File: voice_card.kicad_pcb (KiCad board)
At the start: 2 copper layers, 119.3 x 38 mm, 209 parts, among them J1 PCI_11_49, Q1 MMBF4391LT1G, Q10 DMMT3906, Q11 BC857BS, Q2 2N3904, Q3 BCM847, Q4 DMMT3904, Q5 DMMT3906, Q6 MMBF4391LT1G, Q7 BCM847, Q8 2N3904, Q9 DMMT3904, U1 TL074-, U10 TL072-, U11 TL074-, U12 NE555, U13 LM311M, U14 CD4052, U15 TL072-, U16 TL072-, U17 LM13700, U18 LM13700, U19 LM13700, U2 TL074-, U20 TL072-, U3 NE555, U4 LF351, U5 TL072-, U6 LM311M, U7 CD4052, U8 TL074-, U9 LF351

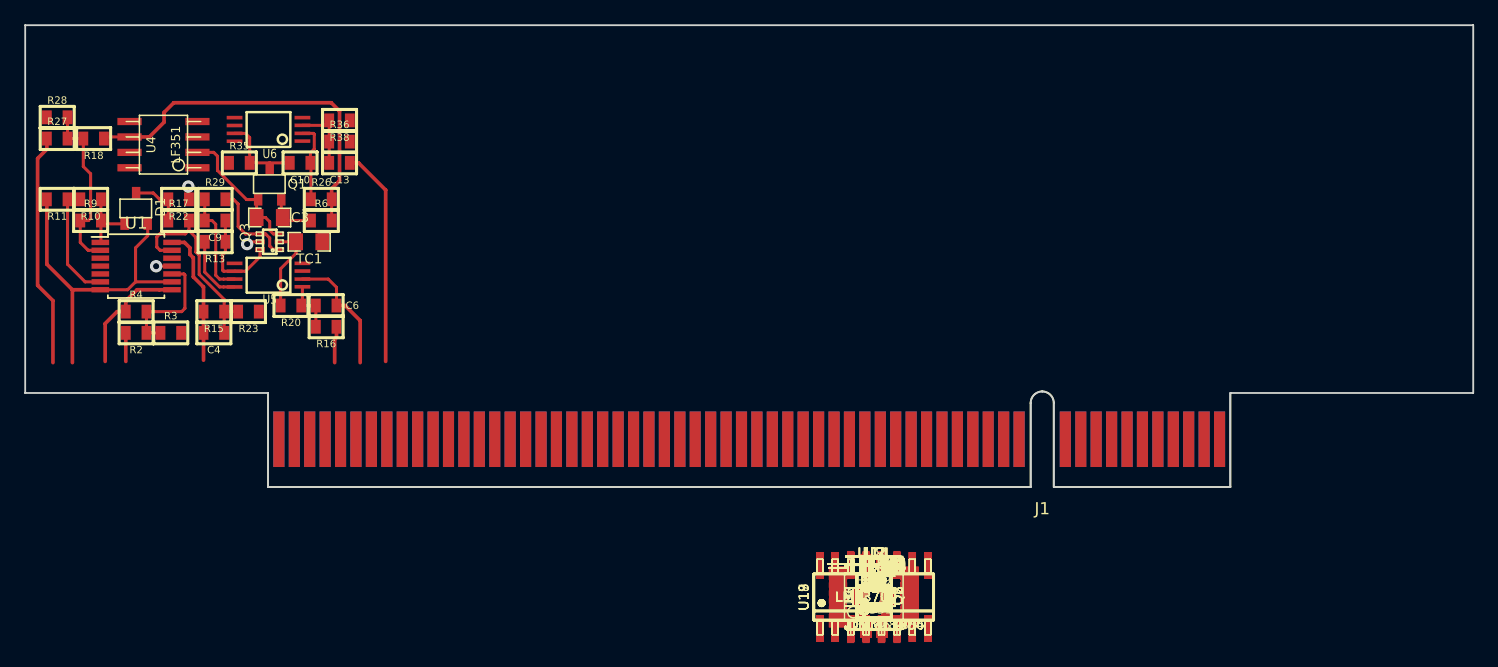
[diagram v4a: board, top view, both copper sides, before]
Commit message: starting to place VCO2 components
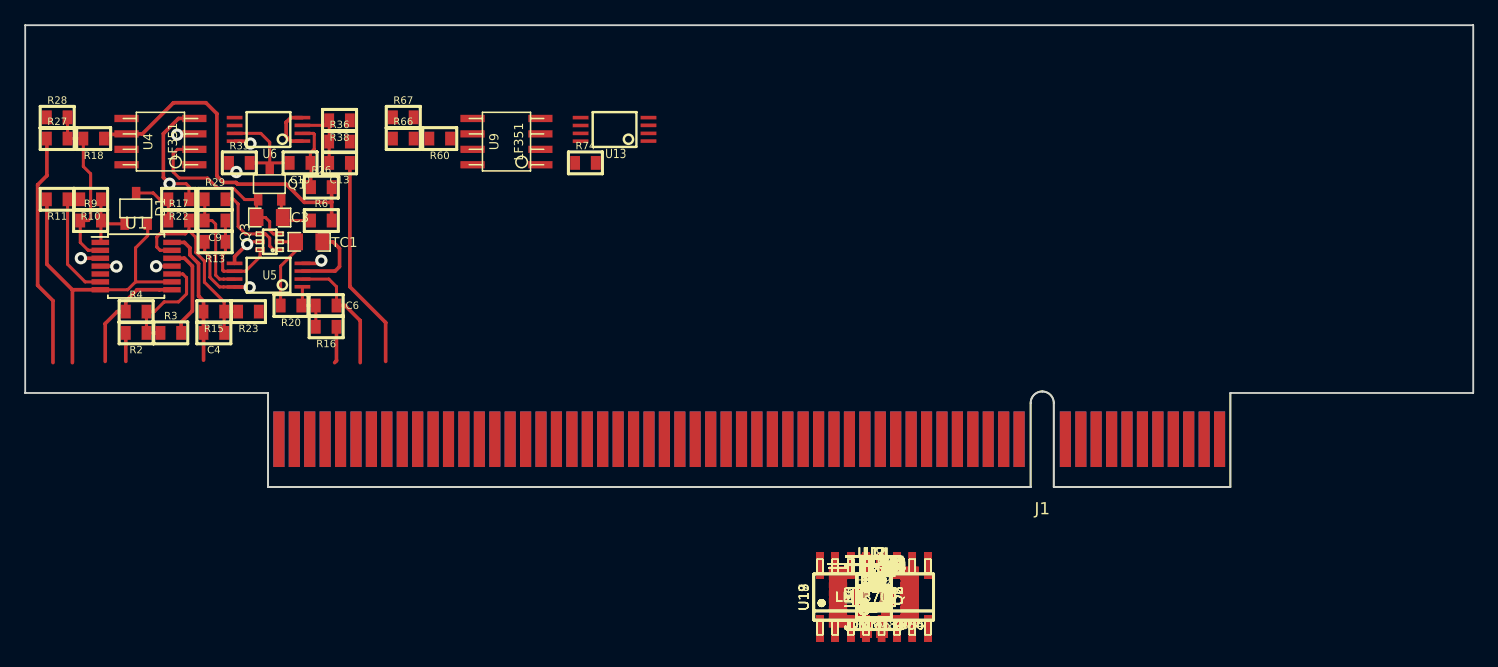
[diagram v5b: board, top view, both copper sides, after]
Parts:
- moved R67 55.3 mm to (109.8, 65.5)
- moved R66 54.1 mm to (109.8, 67.2)
- moved R60 52.0 mm to (112.8, 67.2), turned to 180 degrees
- moved U9 48.2 mm to (118.2, 67.5), turned to 90 degrees
- moved U13 44.0 mm to (127.2, 66.5), turned to 90 degrees
- moved R74 42.9 mm to (124.8, 69.2)
- moved R26 1.00 mm to (103.0, 71.2)
- moved U4 0.35 mm to (89.8, 67.5)
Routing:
- net GND: track 1.14 -> 21.4 mm, vias 1 -> 4
- net -12V: track 2.38 -> 17.3 mm, vias 2 -> 3
- net Net-(C3-Pad1): track 11.7 -> 15.7 mm
- net +12V: track 5.46 -> 9.44 mm, vias 0 -> 3
- net Net-(C10-Pad2): track 7.25 -> 9.32 mm
- net Net-(R18-Pad1): track 30.8 -> 29.3 mm
- net Net-(C10-Pad1): track 6.51 -> 5.51 mm
- net Net-(R2-Pad1): track 10.0 -> 9.47 mm

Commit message: VCO1 and VCO2 rough layout done. Starting to place VCF and VCA components
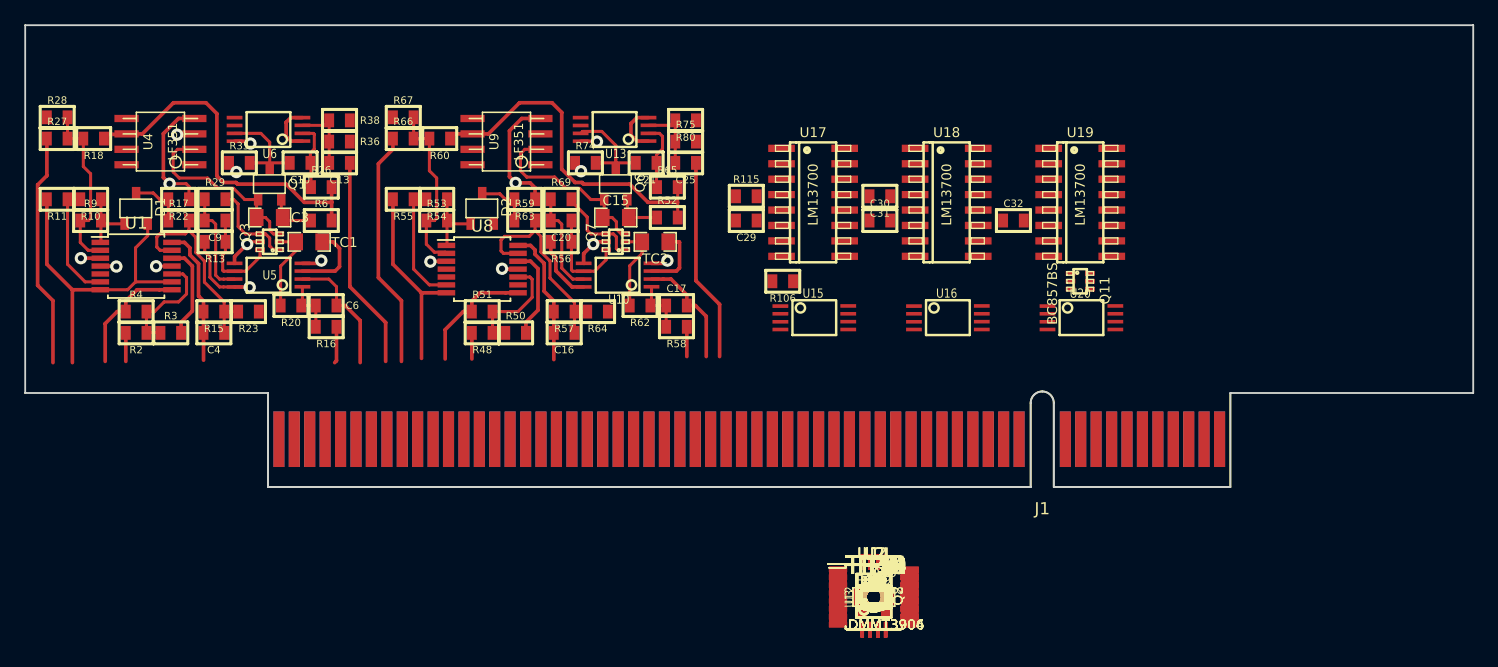
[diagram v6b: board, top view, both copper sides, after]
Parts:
- moved R55 50.7 mm to (109.8, 72.2), turned to 180 degrees
- moved R54 48.7 mm to (112.5, 72.2), turned to 180 degrees
- moved R53 47.5 mm to (112.5, 74.0)
- moved D2 45.4 mm to (116.2, 73.0)
- moved R63 43.6 mm to (119.8, 72.2), turned to 180 degrees
- moved R59 42.3 mm to (119.8, 74.0)
- moved R80 42.2 mm to (133.0, 65.8), turned to 180 degrees
- moved U8 42.1 mm to (116.2, 78.0)
- moved R69 41.7 mm to (122.8, 72.2)
- moved R75 40.6 mm to (133.0, 67.5)
- moved C21 40.4 mm to (129.8, 69.2), turned to 180 degrees
- moved C20 40.3 mm to (122.8, 74.0), turned to 180 degrees
- moved Q6 40.1 mm to (127.2, 71.0)
- moved R51 39.9 mm to (116.2, 81.5)
- moved R56 39.0 mm to (122.8, 75.8), turned to 180 degrees
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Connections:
- U8 pad 10: GND -> Net-(R48-Pad1)
- U8 pad 12: Net-(R48-Pad1) -> GND
- U8 pad 13: VCO2_SAW -> Net-(C16-Pad1)
- U8 pad 14: VCO2_PULSE -> VCO2_TRI
- U8 pad 8: VCO2_TRI -> VCO2_PULSE
- U8 pad 9: Net-(C16-Pad1) -> VCO2_SAW
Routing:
- net Net-(R52-Pad2): track 0.00 -> 29.3 mm
- net VCO2_TRI_SHAPE: track 0.00 -> 19.6 mm
- net GND: track 21.4 -> 39.7 mm, vias 4 -> 7
- net -12V: track 17.3 -> 34.4 mm, vias 3 -> 6
- net Net-(C16-Pad1): track 0.00 -> 17.1 mm
- net VCO2_SYNC_IN: track 0.00 -> 16.8 mm
- net VCO2_SAW: track 0.00 -> 16.1 mm
- net Net-(C15-Pad1): track 0.00 -> 15.4 mm
- net Net-(R53-Pad1): track 0.00 -> 14.7 mm
- net VCO2_TRI: track 0.00 -> 11.2 mm
- net VCO2_PULSE: track 0.00 -> 10.2 mm
- net Net-(R54-Pad2): track 0.00 -> 10.0 mm
- net VCO2_PITCH_CV: track 0.00 -> 9.60 mm
- net Net-(R48-Pad1): track 0.00 -> 9.28 mm
- net Net-(C21-Pad2): track 0.00 -> 9.13 mm
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
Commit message: routing vcf almost done, then need to do VCA and expo converter
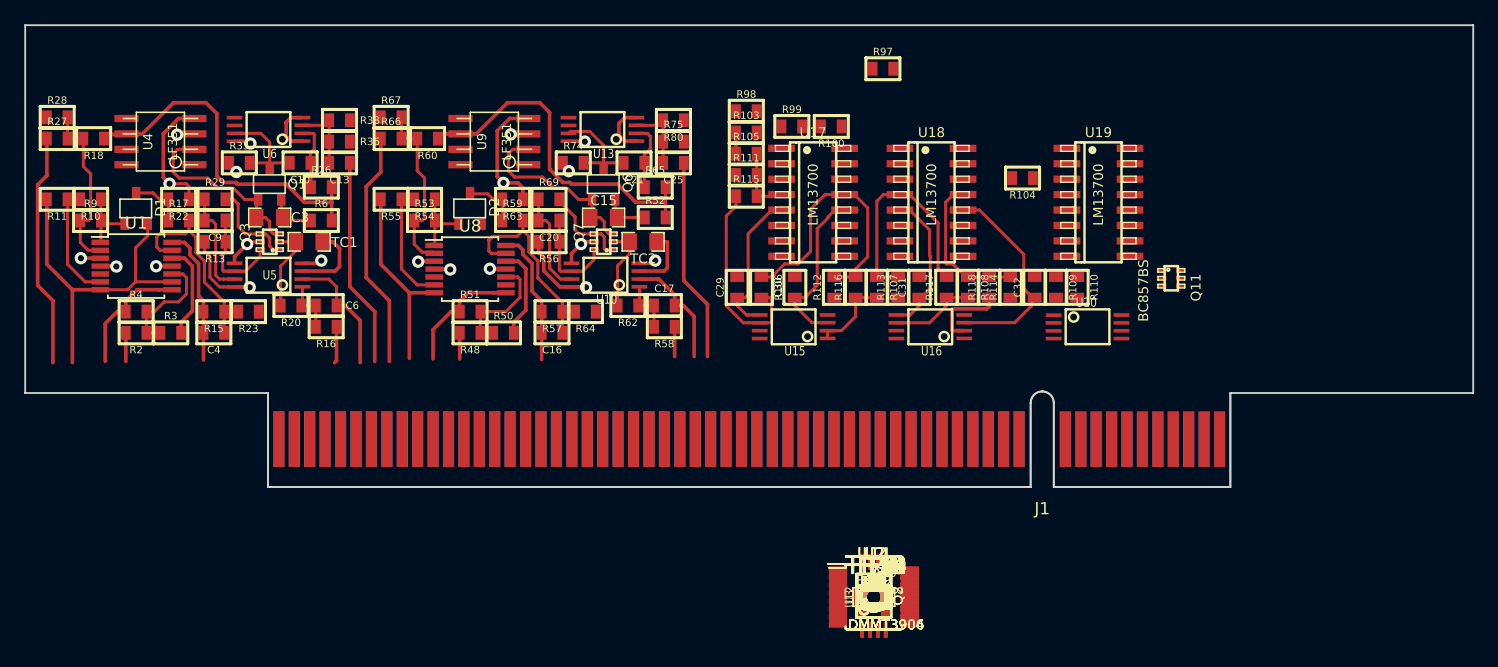
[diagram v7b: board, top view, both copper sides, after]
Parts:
- moved R97 43.5 mm to (149.2, 61.5)
- moved R98 41.4 mm to (138.0, 65.0)
- moved R103 39.7 mm to (138.0, 66.8)
- moved R99 39.3 mm to (141.8, 66.2)
- moved R100 38.9 mm to (145.0, 66.2), turned to 180 degrees
- moved R105 38.0 mm to (138.0, 68.5)
- moved R104 36.6 mm to (160.8, 70.5), turned to 180 degrees
- moved R111 36.3 mm to (138.0, 70.2)
- moved R110 30.5 mm to (165.2, 79.5), turned to 270 degrees
- moved R109 29.6 mm to (163.5, 79.5), turned to 270 degrees
- moved R114 27.9 mm to (159.8, 79.5), turned to 90 degrees
- moved R118 27.2 mm to (158.0, 79.5), turned to 90 degrees
- moved R108 26.7 mm to (156.2, 79.5), turned to 270 degrees
- moved R117 26.2 mm to (154.5, 79.5), turned to 90 degrees
- moved R112 25.7 mm to (145.2, 79.5), turned to 90 degrees
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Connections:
- U15 pad 1: Net-(R106-Pad2) -> Net-(R107-Pad2)
- U15 pad 2: Net-(R106-Pad2) -> Net-(R107-Pad2)
- U15 pad 3: Net-(C29-Pad1) -> Net-(C30-Pad1)
- U15 pad 5: Net-(C30-Pad1) -> Net-(C29-Pad1)
- U15 pad 6: Net-(R107-Pad2) -> Net-(R106-Pad2)
- U15 pad 7: Net-(R107-Pad2) -> Net-(R106-Pad2)
- U16 pad 1: Net-(R108-Pad2) -> VCF_OUT
- U16 pad 2: Net-(R108-Pad2) -> VCF_OUT
- U16 pad 3: Net-(C31-Pad1) -> Net-(C32-Pad1)
- U16 pad 5: Net-(C32-Pad1) -> Net-(C31-Pad1)
- U16 pad 6: VCF_OUT -> Net-(R108-Pad2)
- U16 pad 7: VCF_OUT -> Net-(R108-Pad2)
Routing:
- net Net-(R106-Pad1): track 0.00 -> 21.9 mm
- net Net-(R107-Pad1): track 0.00 -> 19.0 mm
- net Net-(C32-Pad1): track 0.00 -> 18.1 mm
- net Net-(R106-Pad2): track 0.00 -> 16.5 mm
- net Net-(C30-Pad1): track 0.00 -> 14.8 mm
- net Net-(R108-Pad1): track 0.00 -> 12.5 mm
- net Net-(C29-Pad1): track 0.00 -> 12.4 mm
- net Net-(C31-Pad1): track 0.00 -> 12.1 mm
- net Net-(R108-Pad2): track 0.00 -> 7.14 mm
- net Net-(R107-Pad2): track 0.00 -> 6.72 mm
- net VCF_OUT: track 0.00 -> 6.59 mm
- net Net-(R105-Pad2): track 0.00 -> 5.61 mm
- net +12V: track 16.2 -> 18.7 mm, vias 4 -> 6
- net VCF_IN: track 0.00 -> 1.75 mm
- net GND: track 39.7 -> 41.2 mm, vias 7 -> 8

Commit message: finishing up VCF/VCA layout and routing
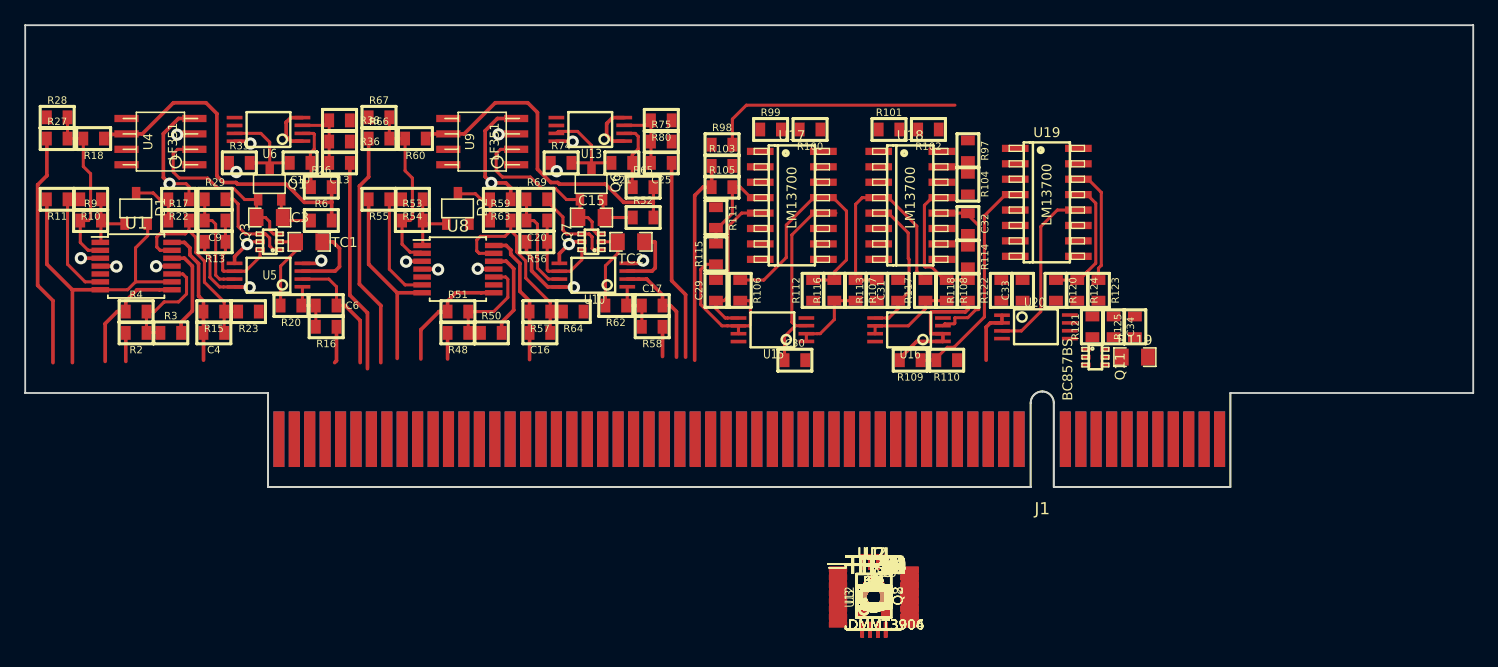
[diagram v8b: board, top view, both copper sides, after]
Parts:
- moved R102 38.8 mm to (153.0, 66.5), turned to 180 degrees
- moved R101 38.5 mm to (149.8, 66.5)
- moved R123 31.3 mm to (167.0, 79.8), turned to 270 degrees
- moved R125 30.9 mm to (170.0, 82.8), turned to 90 degrees
- moved R124 30.3 mm to (165.2, 79.8), turned to 270 degrees
- moved C34 29.8 mm to (168.2, 82.8), turned to 270 degrees
- moved R120 29.4 mm to (163.5, 79.8), turned to 270 degrees
- moved R119 29.2 mm to (170.0, 85.2)
- moved R121 28.6 mm to (166.5, 82.8), turned to 90 degrees
- moved C33 28.1 mm to (160.8, 79.8), turned to 90 degrees
- moved R122 27.3 mm to (159.0, 79.8), turned to 90 degrees
- moved R109 13.4 mm to (151.5, 85.5), turned to 180 degrees
- moved R110 12.3 mm to (154.5, 85.5), turned to 180 degrees
- moved R97 9.72 mm to (156.2, 68.2), turned to 270 degrees
- moved Q11 9.02 mm to (166.8, 85.2)
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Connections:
- U20 pad 1: Net-(C34-Pad1) -> VCA_OUT
- U20 pad 2: Net-(C34-Pad2) -> VCA_OUT
- U20 pad 3: GND -> Net-(C33-Pad1)
- U20 pad 5: Net-(C33-Pad1) -> GND
- U20 pad 6: VCA_OUT -> Net-(C34-Pad2)
- U20 pad 7: VCA_OUT -> Net-(C34-Pad1)
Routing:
- net Net-(R103-Pad2): track 0.00 -> 20.9 mm
- net Net-(R109-Pad1): track 0.00 -> 18.4 mm
- net VCF_IN: track 1.75 -> 17.0 mm
- net Net-(C33-Pad1): track 0.00 -> 14.5 mm
- net Net-(R120-Pad1): track 0.00 -> 11.3 mm
- net Net-(R123-Pad1): track 0.00 -> 9.65 mm
- net VCF_OUT: track 6.59 -> 11.5 mm
- net VCA_OUT: track 0.00 -> 4.81 mm
- net Net-(R106-Pad2): track 16.5 -> 12.6 mm
- net Net-(C32-Pad1): track 18.1 -> 15.0 mm
- net Net-(R105-Pad2): track 5.61 -> 8.16 mm
- net Net-(C30-Pad1): track 14.8 -> 16.1 mm
- net Net-(R108-Pad1): track 12.5 -> 11.8 mm
- net Net-(R108-Pad2): track 7.14 -> 7.79 mm
